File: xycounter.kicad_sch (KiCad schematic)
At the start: 10 parts, among them U1 74LS163, U10 74LS30, U2 74LS163, U3 74LS163, U4 74LS163, U5 74LS163, U6 74LS163, U7 74LS20, U8 74LS14, U9 74LS32

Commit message: fix position counter Y reset logic
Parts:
- added U110, U90: 74LS08, symbol 74xx:74LS08
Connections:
- net +5V: now also U110.14 (VCC)
- net GND: now also U110.7 (GND)
- net ~{ResetY}: now also U90.3; no longer U9.8
- net at U9.3: now also U90.1; no longer U9.9
- net at U9.10: no longer U9.6
- new net: U9.6, U90.2

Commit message: fix x/y counters to reset at the correct positions
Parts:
- removed U7: 74LS20, Package_SO:SO-14_3.9x8.65mm_P1.27mm, symbol 74xx:74LS20
- added U103: 74LS04, symbol 74xx:74LS04
- added U111, U69, U7: 74LS30, symbol 74xx:74LS30
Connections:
- net +5V: now also U111.11, U111.12, U69.14 (VCC), U7.1, U7.14 (VCC), U7.2, U7.3, U7.4, U7.5
- net GND: now also U69.7 (GND), U7.7 (GND)
- net NTSC_RY: now also U7.8
- net PAL_RY: now also U111.8
- net Y0: now also U111.6, U7.6
- net Y1: now also U111.5
- net Y2: now also U111.4, U7.11
- net Y4: now also U111.2
- net Y5: now also U111.1
- net Y8: now also U111.3, U7.12
- net ~{ResetX}: now also U103.9; no longer U4.2 (CP), U5.2 (CP), U6.2 (CP)
- new net ResetX: U103.8, U4.2 (CP), U5.2 (CP), U6.2 (CP)

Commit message: revise position counter
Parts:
- removed unit 2 of U110
- added U19: 74LS32, Package_SO:SO-14_3.9x8.65mm_P1.27mm, symbol 74xx:74LS32
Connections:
- net +5V: now also U2.10 (CET), U3.10 (CET), U5.10 (CET), U6.10 (CET)
- net 14M: no longer U2.2 (CP), U3.2 (CP)
- net CX0: now also U2.2 (CP); no longer U2.10 (CET)
- net CX1: now also U3.2 (CP); no longer U3.10 (CET)
- net CY0: now also U5.2 (CP); no longer U5.10 (CET)
- net CY1: now also U6.2 (CP); no longer U6.10 (CET)
- net ResetX: no longer U5.2 (CP), U6.2 (CP)
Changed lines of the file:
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@@
 	)
 	(junction
+		(at 146.05 157.48)
+		(diameter 0)
+		(color 0 0 0 0)
+	)
+	(junction
+		(at 24.13 157.48)
+		(diameter 0)
+		(color 0 0 0 0)
+	)
+	(junction
 		(at 24.13 95.25)
 		(diameter 0)
@@
 	)
 	(junction
+		(at 24.13 102.87)
+		(diameter 0)
+		(color 0 0 0 0)
+	)
+	(junction
 		(at 146.05 38.1)
 		(diameter 0)
@@
 	)
 	(junction
+		(at 146.05 102.87)
+		(diameter 0)
+		(color 0 0 0 0)
+	)
+	(junction
 		(at 146.05 90.17)
 		(diameter 0)
@@
 		)
 	)
+	(wire
+		(pts
+			(xy 24.13 157.48) (xy 24.13 160.02)
+		)
+		(stroke
+			(width 0)
+			(type default)
+		)
+	)
 	(bus
 		(pts
@@
 	(wire
 		(pts
+			(xy 24.13 102.87) (xy 24.13 105.41)
+		)
+		(stroke
+			(width 0)
+			(type default)
+		)
+	)
+	(wire
+		(pts
 			(xy 207.01 46.99) (xy 210.82 46.99)
 		)
@@
 	(wire
 		(pts
+			(xy 146.05 157.48) (xy 146.05 160.02)
+		)
+		(stroke
+			(width 0)
+			(type default)
+		)
+	)
+	(wire
+		(pts
 			(xy 224.79 46.99) (xy 228.6 46.99)
 		)
@@
 	(wire
 		(pts
+			(xy 146.05 102.87) (xy 146.05 105.41)
+		)
+		(stroke
+			(width 0)
+			(type default)
+		)
+	)
+	(wire
+		(pts
 			(xy 199.39 74.93) (xy 205.74 74.93)
 		)
@@
 		)
 	)
-	(label "CY0"
-		(at 146.05 105.41 180)
-		(effects
-			(font
-				(size 1.27 1.27)
-			)
-			(justify right bottom)
-		)
-	)
 	(label "X1"
 		(at 83.82 41.91 180)
@@
 		)
 	)
-	(label "ResetX"
+	(label "CY0"
 		(at 146.05 107.95 180)
 		(effects
@@
 		)
 	)
-	(label "CY1"
-		(at 146.05 160.02 180)
-		(effects
-			(font
-				(size 1.27 1.27)
-			)
-			(justify right bottom)
-		)
-	)
 	(label "Y6"
 		(at 210.82 46.99 180)
@@
 		)
 	)
-	(label "CX1"
-		(at 24.13 160.02 180)
-		(effects
-			(font
-				(size 1.27 1.27)
-			)
-			(justify right bottom)
-		)
-	)
 	(label "X5"
 		(at 83.82 52.07 180)
@@
 		)
 	)
-	(label "CX0"
-		(at 24.13 105.41 180)
+	(label "CX1"
+		(at 24.13 162.56 180)
 		(effects
 			(font
@@
 		)
 	)
+	(label "CY1"
+		(at 146.05 162.56 180)
+		(effects
+			(font
+				(size 1.27 1.27)
+			)
+			(justify right bottom)
+		)
+	)
 	(label "X2"
 		(at 83.82 44.45 180)
@@
 		)
 	)
-	(label "ResetX"
-		(at 146.05 162.56 180)
-		(effects
-			(font
-				(size 1.27 1.27)
-			)
-			(justify right bottom)
-		)
-	)
 	(label "Y2"
 		(at 210.82 36.83 180)
@@
 		)
 	)
-	(label "X9"
-		(at 49.53 144.78 0)
+	(label "CX0"
+		(at 24.13 107.95 180)
 		(effects
 			(font
 				(size 1.27 1.27)
 			)
-			(justify left bottom)
+			(justify right bottom)
 		)
 	)
-	(global_label "14M"
-		(shape input)
-		(at 24.13 162.56 180)
-		(fields_autoplaced yes)
+	(label "X9"
+		(at 49.53 144.78 0)
 		(effects
 			(font
 				(size 1.27 1.27)
 			)
-			(justify right)
-		)
-		(property "Intersheetrefs" "${INTERSHEET_REFS}"
-			(at 17.2744 162.56 0)
-			(effects
-				(font
-					(size 1.27 1.27)
-				)
-				(justify right)
-				(hide yes)
-			)
+			(justify left bottom)
 		)
 	)
@@
 		)
 	)
-	(global_label "14M"
-		(shape input)
-		(at 24.13 107.95 180)
-		(fields_autoplaced yes)
-		(effects
-			(font
-				(size 1.27 1.27)
-			)
-			(justify right)
-		)
-		(property "Intersheetrefs" "${INTERSHEET_REFS}"
-			(at 17.2744 107.95 0)
-			(effects
-				(font
-					(size 1.27 1.27)
-				)
-				(justify right)
-				(hide yes)
-			)
-		)
-	)
 	(global_label "~{Format}"
 		(shape output)
@@
 	)
 	(symbol
+		(lib_id "74xx:74LS32")
+		(at 312.42 96.52 0)
+		(unit 2)
+		(exclude_from_sim no)
+		(in_bom yes)
+		(on_board yes)
+		(dnp no)
+		(fields_autoplaced yes)
+		(property "Reference" "U19"
+			(at 312.42 87.63 0)
+			(effects
+				(font
+					(size 1.27 1.27)
+				)
+			)
+		)
+		(property "Value" "74LS32"
+			(at 312.42 90.17 0)
+			(effects
+				(font
+					(size 1.27 1.27)
+				)
+			)
+		)
+		(property "Footprint" "Package_SO:SO-14_3.9x8.65mm_P1.27mm"
+			(at 312.42 96.52 0)
+			(effects
+				(font
+					(size 1.27 1.27)
+				)
+				(hide yes)
+			)
+		)
+		(property "Datasheet" "http://www.ti.com/lit/gpn/sn74LS32"
+			(at 312.42 96.52 0)
+			(effects
+				(font
+					(size 1.27 1.27)
+				)
+				(hide yes)
+			)
+		)
+		(property "Description" "Quad 2-input OR"
+			(at 312.42 96.52 0)
+			(effects
+				(font
+					(size 1.27 1.27)
+				)
+				(hide yes)
+			)
+		)
+		(pin "14"
+		)
+		(pin "7"
+		)
+		(pin "2"
+		)
+		(pin "10"
+		)
+		(pin "6"
+		)
+		(pin "8"
+		)
+		(pin "5"
+		)
+		(pin "13"
+		)
+		(pin "12"
+		)
+		(pin "11"
+		)
+		(pin "9"
+		)
+		(pin "4"
+		)
+		(pin "3"
+		)
+		(pin "1"
+		)
+		(instances
+			(project "DIY-Video"
+				(path "/6c4ef05c-ecf5-4bee-ae4e-d72f13738678/f5684949-2fde-4e5d-bf51-2b5a0ce27e60"
+					(reference "U19")
+					(unit 2)
+				)
+			)
+		)
+	)
+	(symbol
 		(lib_id "power:+5V")
 		(at 17.78 48.26 0)
@@
 				)
 			)
-		)
-	)
-	(symbol
-		(lib_id "74xx:74LS08")
-		(at 312.42 96.52 0)
-		(unit 2)
-		(exclude_from_sim no)
-		(in_bom yes)
-		(on_board yes)
-		(dnp no)
-		(fields_autoplaced yes)
-		(property "Reference" "U110"
-			(at 312.4117 87.63 0)
-			(effects
-				(font
-					(size 1.27 1.27)
-				)
-			)
-		)
-		(property "Value" "74LS08"
-			(at 312.4117 90.17 0)
-			(effects
-				(font
-					(size 1.27 1.27)
-				)
-			)
-		)
-		(property "Footprint" ""
-			(at 312.42 96.52 0)
-			(effects
-				(font
-					(size 1.27 1.27)
-				)
-				(hide yes)
-			)
-		)
-		(property "Datasheet" "http://www.ti.com/lit/gpn/sn74LS08"
-			(at 312.42 96.52 0)
-			(effects
-				(font
-					(size 1.27 1.27)
-				)
-				(hide yes)
-			)
-		)
-		(property "Description" "Quad And2"
-			(at 312.42 96.52 0)
-			(effects
-				(font
-					(size 1.27 1.27)
-				)
-				(hide yes)
-			)
-		)
-		(pin "8"
-		)
-		(pin "4"
-		)
-		(pin "5"
-		)
-		(pin "3"
-		)
-		(pin "10"
-		)
-		(pin "1"
-		)
-		(pin "6"
-		)
-		(pin "2"
-		)
-		(pin "9"
-		)
-		(pin "11"
-		)
-		(pin "14"
-		)
-		(pin "12"
-		)
-		(pin "13"
-		)
-		(pin "7"
-		)
-		(instances
-			(project "DIY-Video"
-				(path "/6c4ef05c-ecf5-4bee-ae4e-d72f13738678/f5684949-2fde-4e5d-bf51-2b5a0ce27e60"
-					(reference "U110")
-					(unit 2)
-				)
-			)

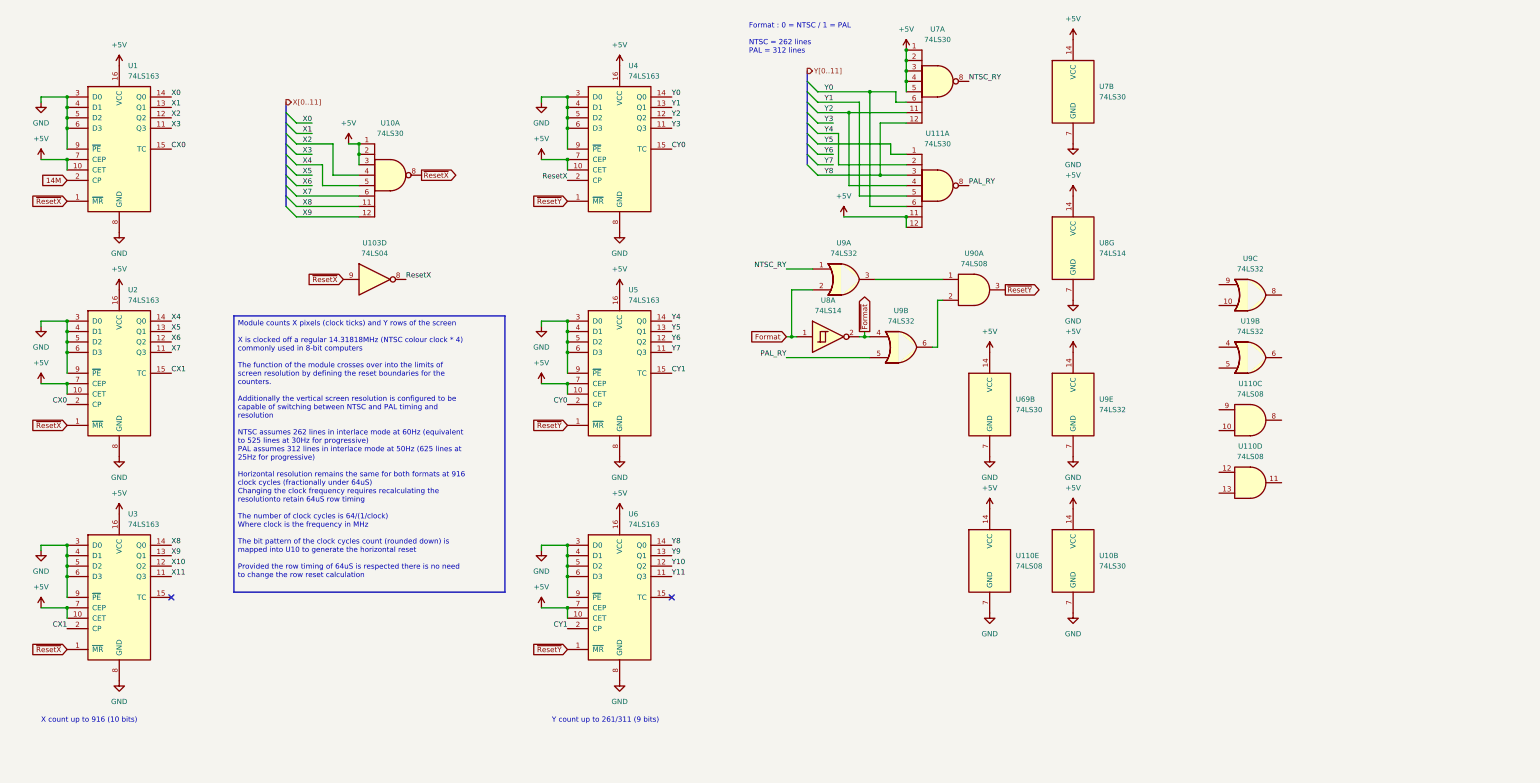
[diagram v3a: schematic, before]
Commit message: isolate each schematic function for testing
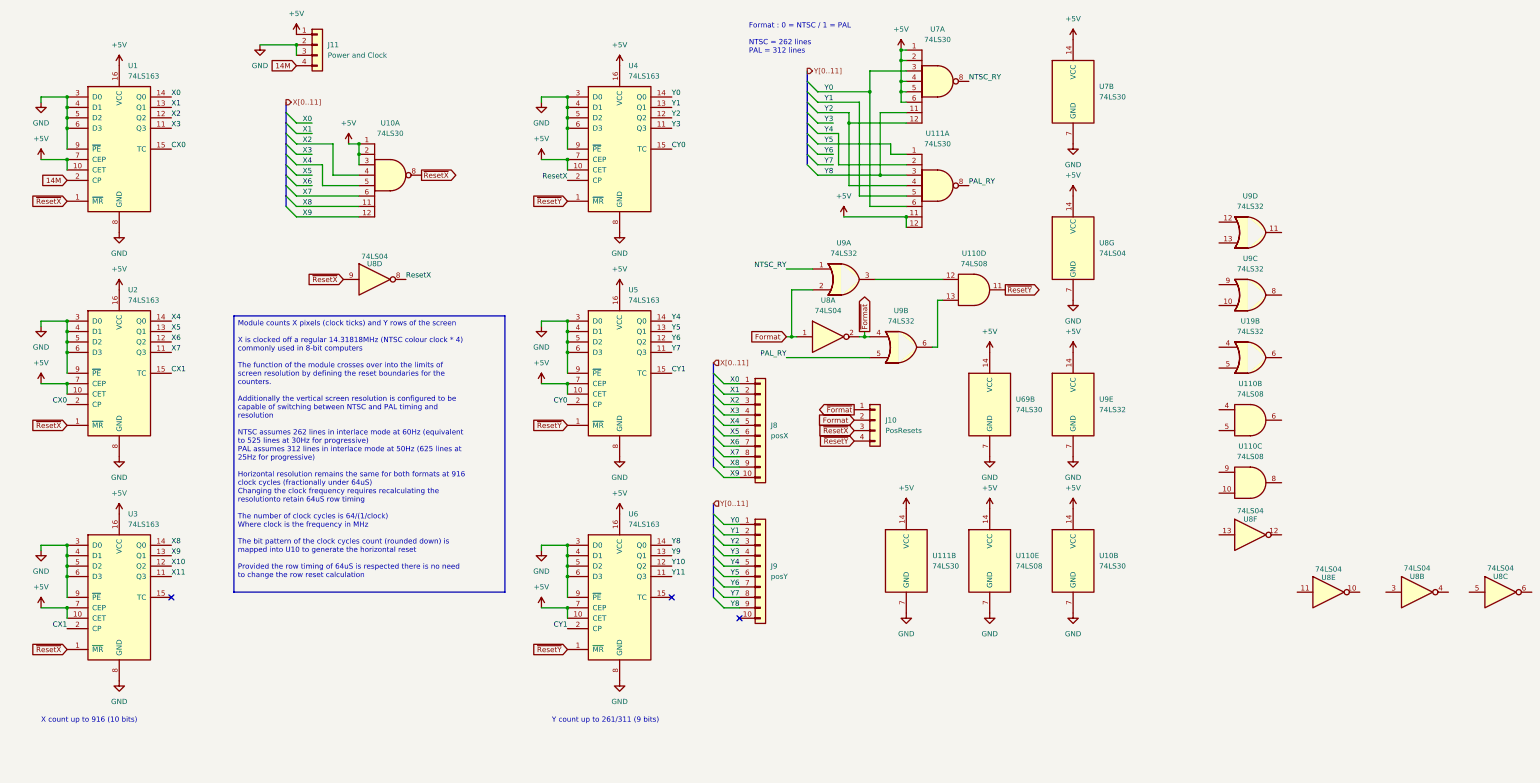
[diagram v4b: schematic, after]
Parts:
- removed U103: 74LS04, symbol 74xx:74LS04
- removed U90: 74LS08, symbol 74xx:74LS08
- added J10: PosResets, Connector_PinSocket_2.54mm:PinSocket_1x04_P2.54mm_Vertical, symbol Connector_Generic:Conn_01x04
- added J11: Power and Clock, Connector_PinSocket_2.54mm:PinSocket_1x04_P2.54mm_Vertical, symbol Connector_Generic:Conn_01x04
- added J8: posX, Connector_PinSocket_2.54mm:PinSocket_1x10_P2.54mm_Vertical, symbol Connector_Generic:Conn_01x10
- added J9: posY, Connector_PinSocket_2.54mm:PinSocket_1x10_P2.54mm_Vertical, symbol Connector_Generic:Conn_01x10
- added unit 2 of U110
- added unit 2 of U111
- added unit 4 of U8
- added unit 5 of U8
- added unit 3 of U8
- added unit 2 of U8
- added unit 6 of U8
- added unit 4 of U9
- U111, U7: footprint (none) -> Package_SO:SO-14_3.9x8.65mm_P1.27mm
- U8: value 74LS14 -> 74LS04; symbol 74xx:74LS14 -> 74xx:74LS04
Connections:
- net +5V: now also U7.6, J11.1 (Pin_1), U111.14 (VCC); no longer U7.3
- net 14M: now also J11.4 (Pin_4)
- net Format: now also J10.2 (Pin_2)
- net GND: now also J11.2 (Pin_2), J11.3 (Pin_3), U111.7 (GND)
- net ResetX: now also U8.8
- net X0: now also J8.1 (Pin_1)
- net X1: now also J8.2 (Pin_2)
- net X2: now also J8.3 (Pin_3)
- net X3: now also J8.4 (Pin_4)
- net X4: now also J8.5 (Pin_5)
- net X5: now also J8.6 (Pin_6)
- net X6: now also J8.7 (Pin_7)
- net X7: now also J8.8 (Pin_8)
- net X8: now also J8.9 (Pin_9)
- net X9: now also J8.10 (Pin_10)
- net Y0: now also U7.3, J9.1 (Pin_1); no longer U7.6
- net Y1: now also J9.2 (Pin_2)
- net Y2: now also U7.12, J9.3 (Pin_3); no longer U7.11
- net Y3: now also J9.4 (Pin_4)
- net Y4: now also J9.5 (Pin_5)
- net Y5: now also J9.6 (Pin_6)
- net Y6: now also J9.7 (Pin_7)
- net Y7: now also J9.8 (Pin_8)
- net Y8: now also U7.11, J9.9 (Pin_9); no longer U7.12
- net ~{Format}: now also J10.1 (Pin_1)
- net ~{ResetX}: now also J10.3 (Pin_3), U8.9
- net ~{ResetY}: now also U110.11, J10.4 (Pin_4)
- net at U9.3: now also U110.12
- net at U9.6: now also U110.13
- no-connect marks 2 -> 3
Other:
- moved on the sheet: U110D

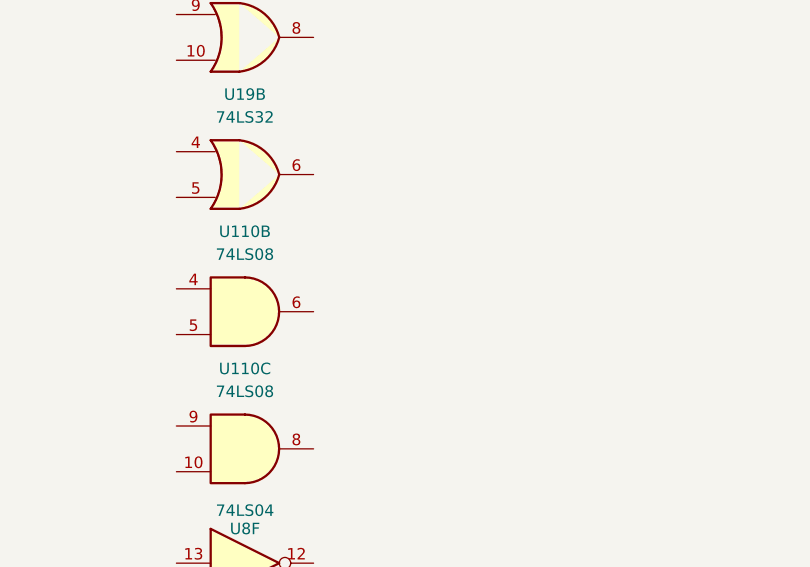
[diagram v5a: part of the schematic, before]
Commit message: spin register out as separate board
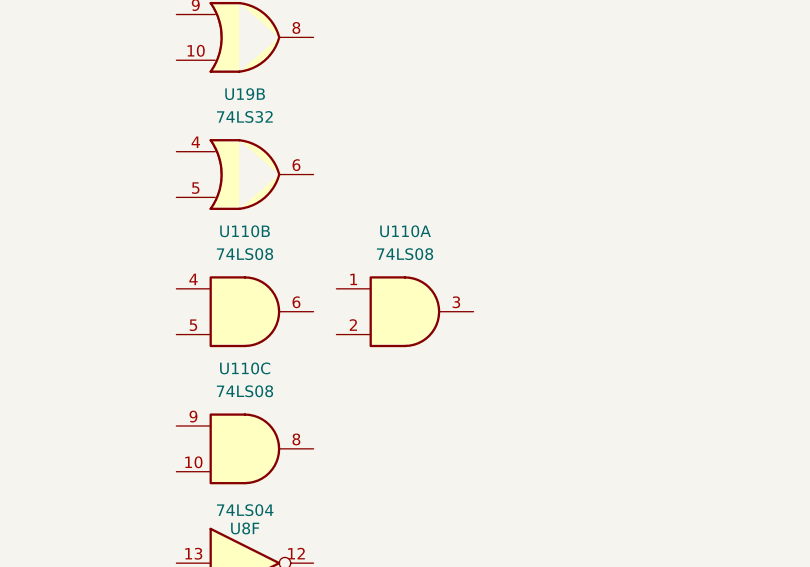
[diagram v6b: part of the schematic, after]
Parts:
- added unit 1 of U110
- U110: footprint (none) -> Package_SO:SO-14_3.9x8.65mm_P1.27mm
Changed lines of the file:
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@@
 			)
 		)
-		(property "Footprint" ""
+		(property "Footprint" "Package_SO:SO-14_3.9x8.65mm_P1.27mm"
 			(at 245.11 80.01 0)
 			(effects
@@
 	)
 	(symbol
+		(lib_id "74xx:74LS08")
+		(at 330.2 111.76 0)
+		(unit 1)
+		(exclude_from_sim no)
+		(in_bom yes)
+		(on_board yes)
+		(dnp no)
+		(fields_autoplaced yes)
+		(property "Reference" "U110"
+			(at 330.1917 102.87 0)
+			(effects
+				(font
+					(size 1.27 1.27)
+				)
+			)
+		)
+		(property "Value" "74LS08"
+			(at 330.1917 105.41 0)
+			(effects
+				(font
+					(size 1.27 1.27)
+				)
+			)
+		)
+		(property "Footprint" "Package_SO:SO-14_3.9x8.65mm_P1.27mm"
+			(at 330.2 111.76 0)
+			(effects
+				(font
+					(size 1.27 1.27)
+				)
+				(hide yes)
+			)
+		)
+		(property "Datasheet" "http://www.ti.com/lit/gpn/sn74LS08"
+			(at 330.2 111.76 0)
+			(effects
+				(font
+					(size 1.27 1.27)
+				)
+				(hide yes)
+			)
+		)
+		(property "Description" "Quad And2"
+			(at 330.2 111.76 0)
+			(effects
+				(font
+					(size 1.27 1.27)
+				)
+				(hide yes)
+			)
+		)
+		(pin "9"
+		)
+		(pin "12"
+		)
+		(pin "7"
+		)
+		(pin "14"
+		)
+		(pin "10"
+		)
+		(pin "1"
+		)
+		(pin "6"
+		)
+		(pin "3"
+		)
+		(pin "13"
+		)
+		(pin "4"
+		)
+		(pin "2"
+		)
+		(pin "5"
+		)
+		(pin "11"
+		)
+		(pin "8"
+		)
+		(instances
+			(project "DIY-Video"
+				(path "/6c4ef05c-ecf5-4bee-ae4e-d72f13738678/f5684949-2fde-4e5d-bf51-2b5a0ce27e60"
+					(reference "U110")
+					(unit 1)
+				)
+			)
+		)
+	)
+	(symbol
 		(lib_id "power:GND")
 		(at 248.92 120.65 0)
@@
 			)
 		)
-		(property "Footprint" ""
+		(property "Footprint" "Package_SO:SO-14_3.9x8.65mm_P1.27mm"
 			(at 312.42 127 0)
 			(effects
@@
 			)
 		)
-		(property "Footprint" ""
+		(property "Footprint" "Package_SO:SO-14_3.9x8.65mm_P1.27mm"
 			(at 312.42 111.76 0)
 			(effects
@@
 			)
 		)
-		(property "Footprint" ""
+		(property "Footprint" "Package_SO:SO-14_3.9x8.65mm_P1.27mm"
 			(at 248.92 146.05 0)
 			(effects

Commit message: refine main board layout
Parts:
- added C1, C10, C11, C12, C2, C3, C4, C5, C6, C7, C8, C9: 10nF, Capacitor_SMD:C_0603_1608Metric, symbol Device:C_Small
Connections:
- net +5V: now also C1.1, C10.1, C11.1, C12.1, C2.1, C3.1, C4.1, C5.1, C6.1, C7.1, C8.1, C9.1
- net GND: now also C1.2, C10.2, C11.2, C12.2, C2.2, C3.2, C4.2, C5.2, C6.2, C7.2, C8.2, C9.2
